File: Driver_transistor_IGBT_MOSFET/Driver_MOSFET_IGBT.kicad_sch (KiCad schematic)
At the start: 12 parts, among them J3 Conn_01x02, J4 Conn_01x02, J5 Conn_01x01, Q5 IRF830, Q6 IRF830, Q7 IRG4BC30, T1 1:1

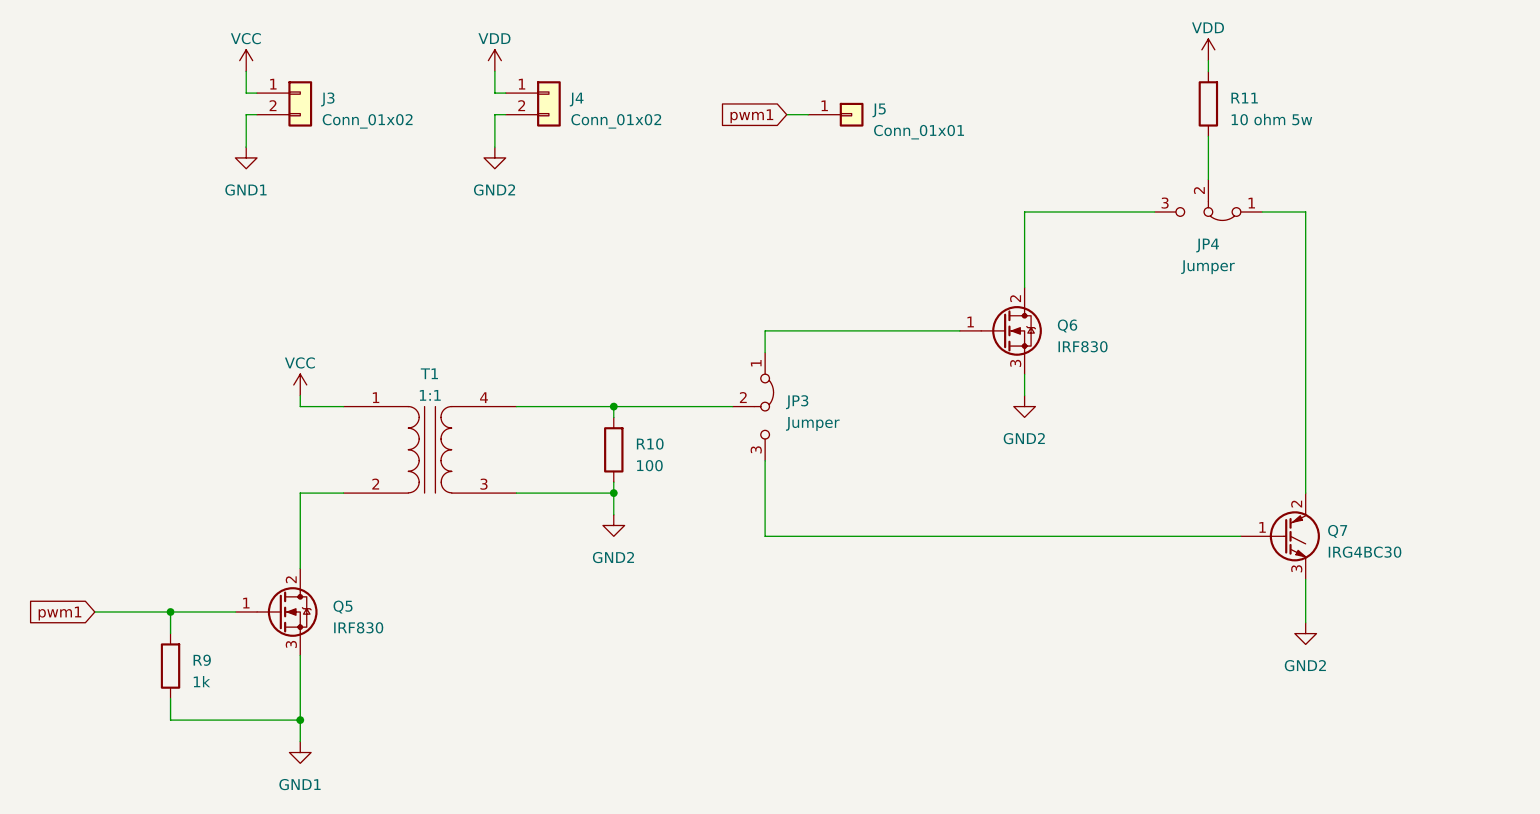
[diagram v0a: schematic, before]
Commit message: rediseño driver IGBT-MOSFET
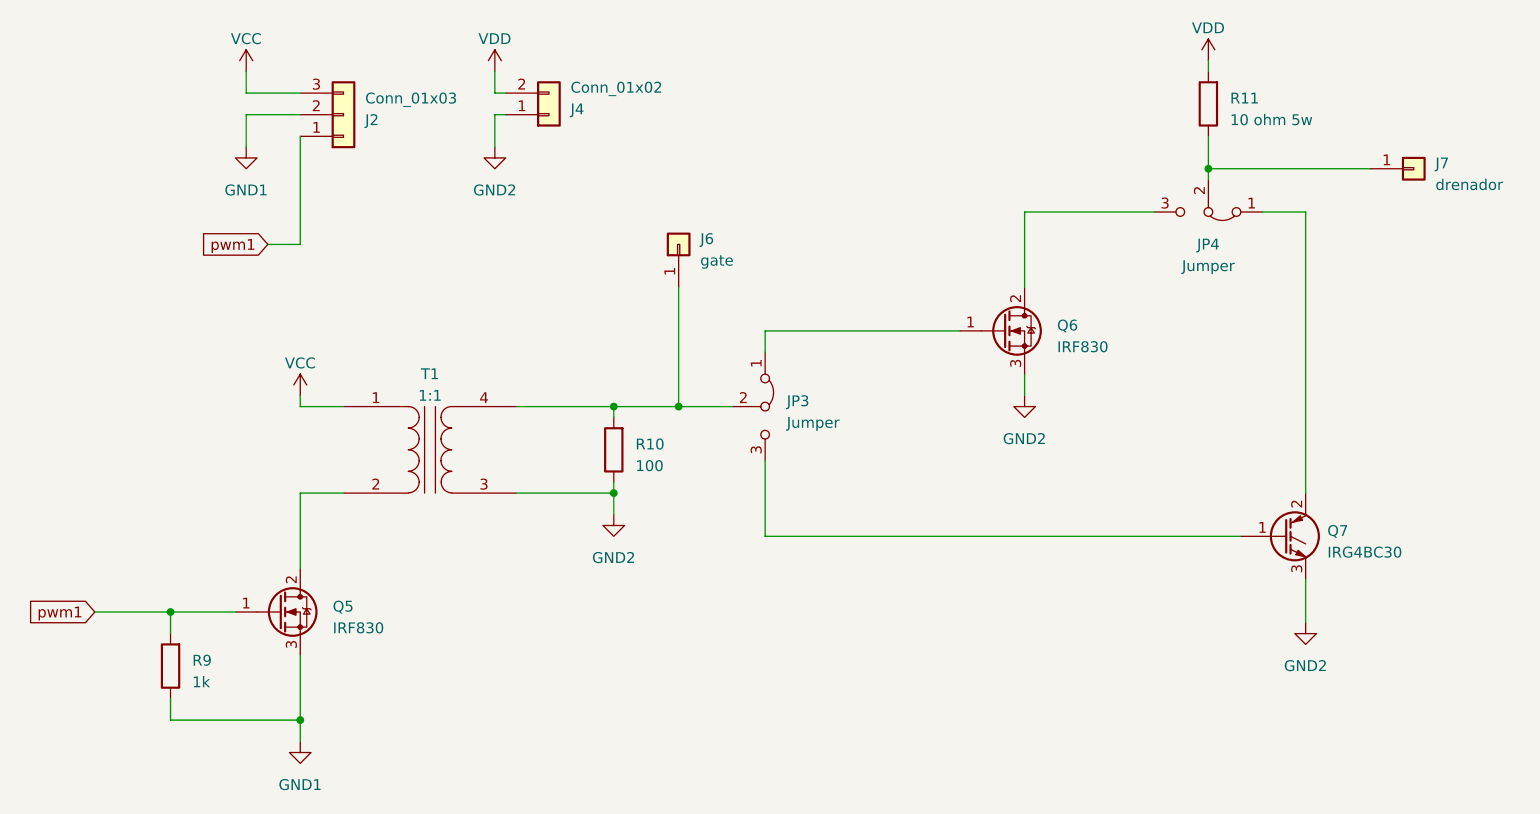
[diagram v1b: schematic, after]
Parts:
- removed J3: Conn_01x02, Connector_Wire:SolderWire-0.5sqmm_1x02_P4.6mm_D0.9mm_OD2.1mm, symbol Connector_Generic:Conn_01x02
- removed J5: Conn_01x01, Connector_PinHeader_2.00mm:PinHeader_1x01_P2.00mm_Vertical, symbol Connector_Generic:Conn_01x01
- added J2: Conn_01x03, TerminalBlock_Altech:Altech_AK300_1x03_P5.00mm_45-Degree, symbol Connector_Generic:Conn_01x03
- added J6: gate, Connector_PinHeader_2.00mm:PinHeader_1x01_P2.00mm_Vertical, symbol Connector_Generic:Conn_01x01
- added J7: drenador, Connector_PinHeader_2.00mm:PinHeader_1x01_P2.00mm_Vertical, symbol Connector_Generic:Conn_01x01
- J4: footprint Connector_Wire:SolderWire-0.5sqmm_1x02_P4.6mm_D0.9mm_OD2.1mm -> TerminalBlock_Altech:Altech_AK300_1x02_P5.00mm_45-Degree
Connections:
- net GND1: now also J2.2 (Pin_2)
- net GND2: now also J4.1 (Pin_1); no longer J4.2 (Pin_2)
- net VCC: now also J2.3 (Pin_3)
- net VDD: now also J4.2 (Pin_2); no longer J4.1 (Pin_1)
- net pwm1: now also J2.1 (Pin_1)
- net at JP3.2 (C), R10.2, T1.4 (SB): now also J6.1 (Pin_1)
- net at JP4.2 (C), R11.1: now also J7.1 (Pin_1)
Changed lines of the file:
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@@
   (junction (at 95.25 127) (diameter 0) (color 0 0 0 0)
   )
+  (junction (at 139.7 90.17) (diameter 0) (color 0 0 0 0)
+  )
   (junction (at 80.01 114.3) (diameter 0) (color 0 0 0 0)
   )
+  (junction (at 201.93 62.23) (diameter 0) (color 0 0 0 0)
+  )
   (junction (at 132.08 90.17) (diameter 0) (color 0 0 0 0)
   )
-  (wire (pts (xy 201.93 58.42) (xy 201.93 63.5))
+  (wire (pts (xy 201.93 62.23) (xy 201.93 63.5))
+    (stroke (width 0) (type default))
+  )
+  (wire (pts (xy 201.93 58.42) (xy 201.93 62.23))
+    (stroke (width 0) (type default))
+  )
+  (wire (pts (xy 139.7 90.17) (xy 146.05 90.17))
+    (stroke (width 0) (type default))
+  )
+  (wire (pts (xy 88.9 53.34) (xy 95.25 53.34))
     (stroke (width 0) (type default))
   )
@@
     (stroke (width 0) (type default))
   )
+  (wire (pts (xy 201.93 62.23) (xy 220.98 62.23))
+    (stroke (width 0) (type default))
+  )
   (wire (pts (xy 95.25 119.38) (xy 95.25 127))
     (stroke (width 0) (type default))
   )
-  (wire (pts (xy 132.08 90.17) (xy 146.05 90.17))
+  (wire (pts (xy 132.08 90.17) (xy 139.7 90.17))
     (stroke (width 0) (type default))
   )
@@
     (stroke (width 0) (type default))
   )
-  (wire (pts (xy 90.17 53.34) (xy 88.9 53.34))
-    (stroke (width 0) (type default))
-  )
   (wire (pts (xy 201.93 49.53) (xy 201.93 50.8))
     (stroke (width 0) (type default))
   )
-  (wire (pts (xy 119.38 55.88) (xy 118.11 55.88))
-    (stroke (width 0) (type default))
-  )
   (wire (pts (xy 172.72 81.28) (xy 149.86 81.28))
     (stroke (width 0) (type default))
   )
+  (wire (pts (xy 95.25 58.42) (xy 95.25 71.12))
+    (stroke (width 0) (type default))
+  )
+  (wire (pts (xy 118.11 53.34) (xy 119.38 53.34))
+    (stroke (width 0) (type default))
+  )
   (wire (pts (xy 95.25 127) (xy 95.25 129.54))
     (stroke (width 0) (type default))
@@
     (stroke (width 0) (type default))
   )
+  (wire (pts (xy 88.9 55.88) (xy 95.25 55.88))
+    (stroke (width 0) (type default))
+  )
   (wire (pts (xy 120.65 100.33) (xy 132.08 100.33))
     (stroke (width 0) (type default))
@@
     (stroke (width 0) (type default))
   )
-  (wire (pts (xy 119.38 53.34) (xy 118.11 53.34))
-    (stroke (width 0) (type default))
-  )
   (wire (pts (xy 71.12 114.3) (xy 80.01 114.3))
     (stroke (width 0) (type default))
@@
     (stroke (width 0) (type default))
   )
-  (wire (pts (xy 90.17 55.88) (xy 88.9 55.88))
+  (wire (pts (xy 139.7 76.2) (xy 139.7 90.17))
     (stroke (width 0) (type default))
   )
@@
     (stroke (width 0) (type default))
   )
+  (wire (pts (xy 91.44 71.12) (xy 95.25 71.12))
+    (stroke (width 0) (type default))
+  )
   (wire (pts (xy 180.34 86.36) (xy 180.34 88.9))
     (stroke (width 0) (type default))
@@
     (stroke (width 0) (type default))
   )
+  (wire (pts (xy 118.11 55.88) (xy 119.38 55.88))
+    (stroke (width 0) (type default))
+  )
   (wire (pts (xy 95.25 88.9) (xy 95.25 90.17))
     (stroke (width 0) (type default))
@@
     (stroke (width 0) (type default))
   )
-  (wire (pts (xy 152.4 55.88) (xy 154.94 55.88))
-    (stroke (width 0) (type default))
-  )
-  (global_label "pwm1" (shape input) (at 152.4 55.88 180) (fields_autoplaced)
+  (global_label "pwm1" (shape input) (at 91.44 71.12 180) (fields_autoplaced)
     (effects (font (size 1.27 1.27)) (justify right))
-    (property "Intersheetrefs" "${INTERSHEET_REFS}" (at 144.1119 55.88 0)
+    (property "Intersheetrefs" "${INTERSHEET_REFS}" (at 83.1519 71.12 0)
       (effects (font (size 1.27 1.27)) (justify right) hide)
     )
@@
     )
   )
+  (symbol (lib_id "Connector_Generic:Conn_01x01") (at 139.7 71.12 90) (unit 1)
+    (in_bom yes) (on_board yes) (dnp no) (fields_autoplaced)
+    (property "Reference" "J6" (at 142.24 70.485 90)
+      (effects (font (size 1.27 1.27)) (justify right))
+    )
+    (property "Value" "gate" (at 142.24 73.025 90)
+      (effects (font (size 1.27 1.27)) (justify right))
+    )
+    (property "Footprint" "Connector_PinHeader_2.00mm:PinHeader_1x01_P2.00mm_Vertical" (at 139.7 71.12 0)
+      (effects (font (size 1.27 1.27)) hide)
+    )
+    (property "Datasheet" "~" (at 139.7 71.12 0)
+      (effects (font (size 1.27 1.27)) hide)
+    )
+    (pin "1")
+    (instances
+      (project "Driver_transistor"
+        (path "/e4287a4b-c4f2-447b-b63a-9e2c3468b7f7/6929754e-424a-481e-b4f0-ed85c2c964a7"
+          (reference "J6") (unit 1)
+        )
+      )
+    )
+  )
   (symbol (lib_id "power:GND2") (at 118.11 59.69 0) (unit 1)
     (in_bom yes) (on_board yes) (dnp no) (fields_autoplaced)
@@
     )
   )
-  (symbol (lib_id "Connector_Generic:Conn_01x02") (at 124.46 53.34 0) (unit 1)
-    (in_bom yes) (on_board yes) (dnp no) (fields_autoplaced)
-    (property "Reference" "J4" (at 127 53.975 0)
-      (effects (font (size 1.27 1.27)) (justify left))
-    )
-    (property "Value" "Conn_01x02" (at 127 56.515 0)
-      (effects (font (size 1.27 1.27)) (justify left))
-    )
-    (property "Footprint" "Connector_Wire:SolderWire-0.5sqmm_1x02_P4.6mm_D0.9mm_OD2.1mm" (at 124.46 53.34 0)
-      (effects (font (size 1.27 1.27)) hide)
-    )
-    (property "Datasheet" "~" (at 124.46 53.34 0)
+  (symbol (lib_id "Connector_Generic:Conn_01x02") (at 124.46 55.88 0) (mirror x) (unit 1)
+    (in_bom yes) (on_board yes) (dnp no)
+    (property "Reference" "J4" (at 127 55.245 0)
+      (effects (font (size 1.27 1.27)) (justify left))
+    )
+    (property "Value" "Conn_01x02" (at 127 52.705 0)
+      (effects (font (size 1.27 1.27)) (justify left))
+    )
+    (property "Footprint" "TerminalBlock_Altech:Altech_AK300_1x02_P5.00mm_45-Degree" (at 124.46 55.88 0)
+      (effects (font (size 1.27 1.27)) hide)
+    )
+    (property "Datasheet" "~" (at 124.46 55.88 0)
       (effects (font (size 1.27 1.27)) hide)
     )
@@
     )
   )
-  (symbol (lib_id "Connector_Generic:Conn_01x01") (at 160.02 55.88 0) (unit 1)
-    (in_bom yes) (on_board yes) (dnp no) (fields_autoplaced)
-    (property "Reference" "J5" (at 162.56 55.245 0)
-      (effects (font (size 1.27 1.27)) (justify left))
-    )
-    (property "Value" "Conn_01x01" (at 162.56 57.785 0)
-      (effects (font (size 1.27 1.27)) (justify left))
-    )
-    (property "Footprint" "Connector_PinHeader_2.00mm:PinHeader_1x01_P2.00mm_Vertical" (at 160.02 55.88 0)
-      (effects (font (size 1.27 1.27)) hide)
-    )
-    (property "Datasheet" "~" (at 160.02 55.88 0)
-      (effects (font (size 1.27 1.27)) hide)
-    )
-    (pin "1")
-    (instances
-      (project "Driver_transistor"
-        (path "/e4287a4b-c4f2-447b-b63a-9e2c3468b7f7/6929754e-424a-481e-b4f0-ed85c2c964a7"
-          (reference "J5") (unit 1)
-        )
-      )
-    )
-  )
   (symbol (lib_id "power:VCC") (at 95.25 88.9 0) (unit 1)
     (in_bom yes) (on_board yes) (dnp no) (fields_autoplaced)
@@
     )
   )
+  (symbol (lib_id "Connector_Generic:Conn_01x01") (at 226.06 62.23 0) (unit 1)
+    (in_bom yes) (on_board yes) (dnp no) (fields_autoplaced)
+    (property "Reference" "J7" (at 228.6 61.595 0)
+      (effects (font (size 1.27 1.27)) (justify left))
+    )
+    (property "Value" "drenador" (at 228.6 64.135 0)
+      (effects (font (size 1.27 1.27)) (justify left))
+    )
+    (property "Footprint" "Connector_PinHeader_2.00mm:PinHeader_1x01_P2.00mm_Vertical" (at 226.06 62.23 0)
+      (effects (font (size 1.27 1.27)) hide)
+    )
+    (property "Datasheet" "~" (at 226.06 62.23 0)
+      (effects (font (size 1.27 1.27)) hide)
+    )
+    (pin "1")
+    (instances
+      (project "Driver_transistor"
+        (path "/e4287a4b-c4f2-447b-b63a-9e2c3468b7f7/6929754e-424a-481e-b4f0-ed85c2c964a7"
+          (reference "J7") (unit 1)
+        )
+      )
+    )
+  )
   (symbol (lib_id "power:GND2") (at 180.34 88.9 0) (unit 1)
     (in_bom yes) (on_board yes) (dnp no) (fields_autoplaced)
@@
         (path "/e4287a4b-c4f2-447b-b63a-9e2c3468b7f7/6929754e-424a-481e-b4f0-ed85c2c964a7"
           (reference "#PWR013") (unit 1)
+        )
+      )
+    )
+  )
+  (symbol (lib_id "Connector_Generic:Conn_01x03") (at 100.33 55.88 0) (mirror x) (unit 1)
+    (in_bom yes) (on_board yes) (dnp no)
+    (property "Reference" "J2" (at 102.87 56.515 0)
+      (effects (font (size 1.27 1.27)) (justify left))
+    )
+    (property "Value" "Conn_01x03" (at 102.87 53.975 0)
+      (effects (font (size 1.27 1.27)) (justify left))
+    )
+    (property "Footprint" "TerminalBlock_Altech:Altech_AK300_1x03_P5.00mm_45-Degree" (at 100.33 55.88 0)
+      (effects (font (size 1.27 1.27)) hide)
+    )
+    (property "Datasheet" "~" (at 100.33 55.88 0)
+      (effects (font (size 1.27 1.27)) hide)
+    )
+    (pin "1")
+    (pin "2")
+    (pin "3")
+    (instances
+      (project "Driver_transistor"
+        (path "/e4287a4b-c4f2-447b-b63a-9e2c3468b7f7"
+          (reference "J2") (unit 1)
+        )
+        (path "/e4287a4b-c4f2-447b-b63a-9e2c3468b7f7/6929754e-424a-481e-b4f0-ed85c2c964a7"
+          (reference "J8") (unit 1)
         )
       )
@@
         )
       )
-    )
-  )
-  (symbol (lib_id "Connector_Generic:Conn_01x02") (at 95.25 53.34 0) (unit 1)
-    (in_bom yes) (on_board yes) (dnp no) (fields_autoplaced)
-    (property "Reference" "J3" (at 97.79 53.975 0)
-      (effects (font (size 1.27 1.27)) (justify left))
-    )
-    (property "Value" "Conn_01x02" (at 97.79 56.515 0)
-      (effects (font (size 1.27 1.27)) (justify left))
-    )
-    (property "Footprint" "Connector_Wire:SolderWire-0.5sqmm_1x02_P4.6mm_D0.9mm_OD2.1mm" (at 95.25 53.34 0)
-      (effects (font (size 1.27 1.27)) hide)
-    )
-    (property "Datasheet" "~" (at 95.25 53.34 0)
-      (effects (font (size 1.27 1.27)) hide)
-    )
-    (pin "1")
-    (pin "2")
-    (instances
-      (project "Driver_transistor"
-        (path "/e4287a4b-c4f2-447b-b63a-9e2c3468b7f7/6929754e-424a-481e-b4f0-ed85c2c964a7"
-          (reference "J3") (unit 1)
-        )
-      )

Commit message: para vos juan
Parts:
- added J3: surtidor, Connector_PinHeader_2.00mm:PinHeader_1x01_P2.00mm_Vertical, symbol Connector_Generic:Conn_01x01
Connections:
- net GND2: now also J3.1 (Pin_1)
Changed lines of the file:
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@@
   (junction (at 132.08 100.33) (diameter 0) (color 0 0 0 0)
   )
+  (junction (at 180.34 87.63) (diameter 0) (color 0 0 0 0)
+  )
   (junction (at 95.25 127) (diameter 0) (color 0 0 0 0)
   )
@@
     (stroke (width 0) (type default))
   )
+  (wire (pts (xy 180.34 87.63) (xy 180.34 88.9))
+    (stroke (width 0) (type default))
+  )
   (wire (pts (xy 120.65 100.33) (xy 132.08 100.33))
     (stroke (width 0) (type default))
@@
     (stroke (width 0) (type default))
   )
-  (wire (pts (xy 180.34 86.36) (xy 180.34 88.9))
+  (wire (pts (xy 180.34 86.36) (xy 180.34 87.63))
     (stroke (width 0) (type default))
   )
@@
   )
   (wire (pts (xy 208.28 67.31) (xy 213.36 67.31))
+    (stroke (width 0) (type default))
+  )
+  (wire (pts (xy 180.34 87.63) (xy 187.96 87.63))
     (stroke (width 0) (type default))
   )
@@
         )
       )
+    )
+  )
+  (symbol (lib_id "Connector_Generic:Conn_01x01") (at 193.04 87.63 0) (unit 1)
+    (in_bom yes) (on_board yes) (dnp no) (fields_autoplaced)
+    (property "Reference" "J3" (at 195.58 86.995 0)
+      (effects (font (size 1.27 1.27)) (justify left))
+    )
+    (property "Value" "surtidor" (at 195.58 89.535 0)
+      (effects (font (size 1.27 1.27)) (justify left))
+    )
+    (property "Footprint" "Connector_PinHeader_2.00mm:PinHeader_1x01_P2.00mm_Vertical" (at 193.04 87.63 0)
+      (effects (font (size 1.27 1.27)) hide)
+    )
+    (property "Datasheet" "~" (at 193.04 87.63 0)
+      (effects (font (size 1.27 1.27)) hide)
+    )
+    (pin "1")
+    (instances
+      (project "Driver_transistor"
+        (path "/e4287a4b-c4f2-447b-b63a-9e2c3468b7f7/6929754e-424a-481e-b4f0-ed85c2c964a7"
+          (reference "J3") (unit 1)
+        )
+      )
